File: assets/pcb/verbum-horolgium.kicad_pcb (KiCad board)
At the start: 2 copper layers, 100 x 100 mm, 33 parts, among them J1 GND, J2 +5V, J3 LED_DATA, J4 TOUCH, J5 POWER (6-32V), J6 POWER (6-32V), U1 AP63205WU-7

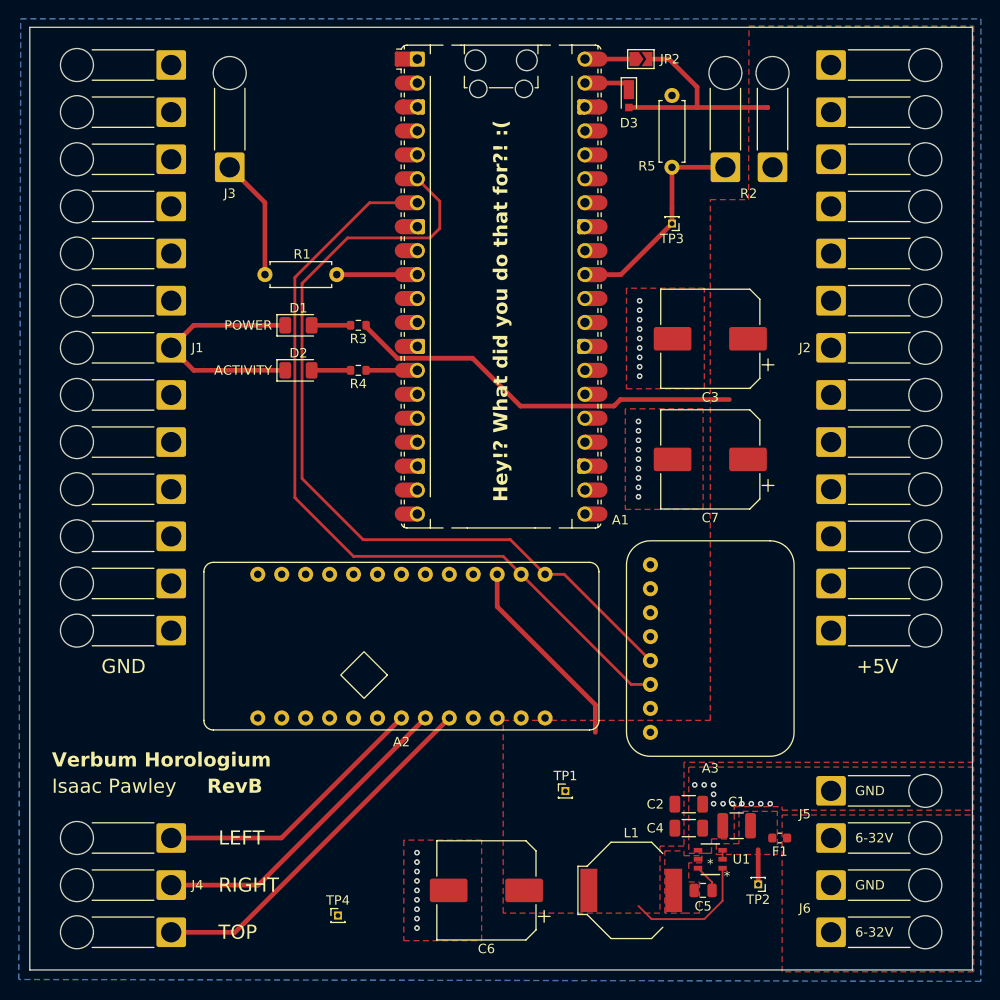
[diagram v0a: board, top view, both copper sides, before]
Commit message: fix: added mounting holes
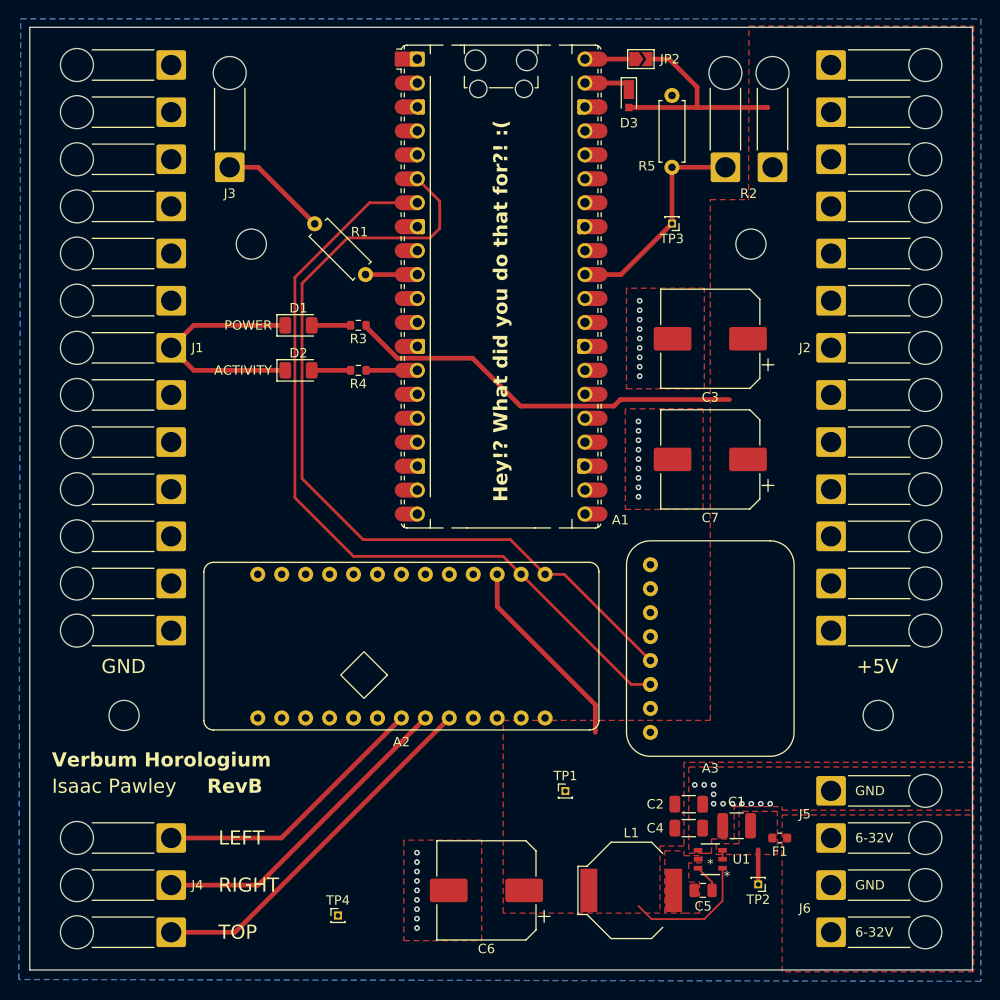
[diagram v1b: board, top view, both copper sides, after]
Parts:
- added H1: MountingHole, MountingHole:MountingHole_3.2mm_M3, F.Cu at (108.5, 128.0)
- added H2: MountingHole, MountingHole:MountingHole_3.2mm_M3, F.Cu at (188.5, 128.0)
- added H3: MountingHole, MountingHole:MountingHole_3.2mm_M3, B.Cu at (122.0, 78.0)
- added H4: MountingHole, MountingHole:MountingHole_3.2mm_M3, F.Cu at (175.0, 78.0)
- moved R1 3.05 mm to (134.1, 81.2), turned to 135 degrees
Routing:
- net /LED_DATA: track 8.55 -> 5.50 mm
- net Net-(J3-Pin_1): track 12.9 -> 11.5 mm
